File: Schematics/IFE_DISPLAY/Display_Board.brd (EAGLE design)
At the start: 108 x 83.8 mm, 76 parts, among them IC2 EP2C5T144, Q1 16MHz, Q2 MMBT3904L, Q3 16MHz, U1 MCP1826S-1802E/DB, U10 TPS5420D, U2 EPCS1SI8N, U4 HEX_CONVERTER, U5 HEX_CONVERTER, U9 TPS5420D

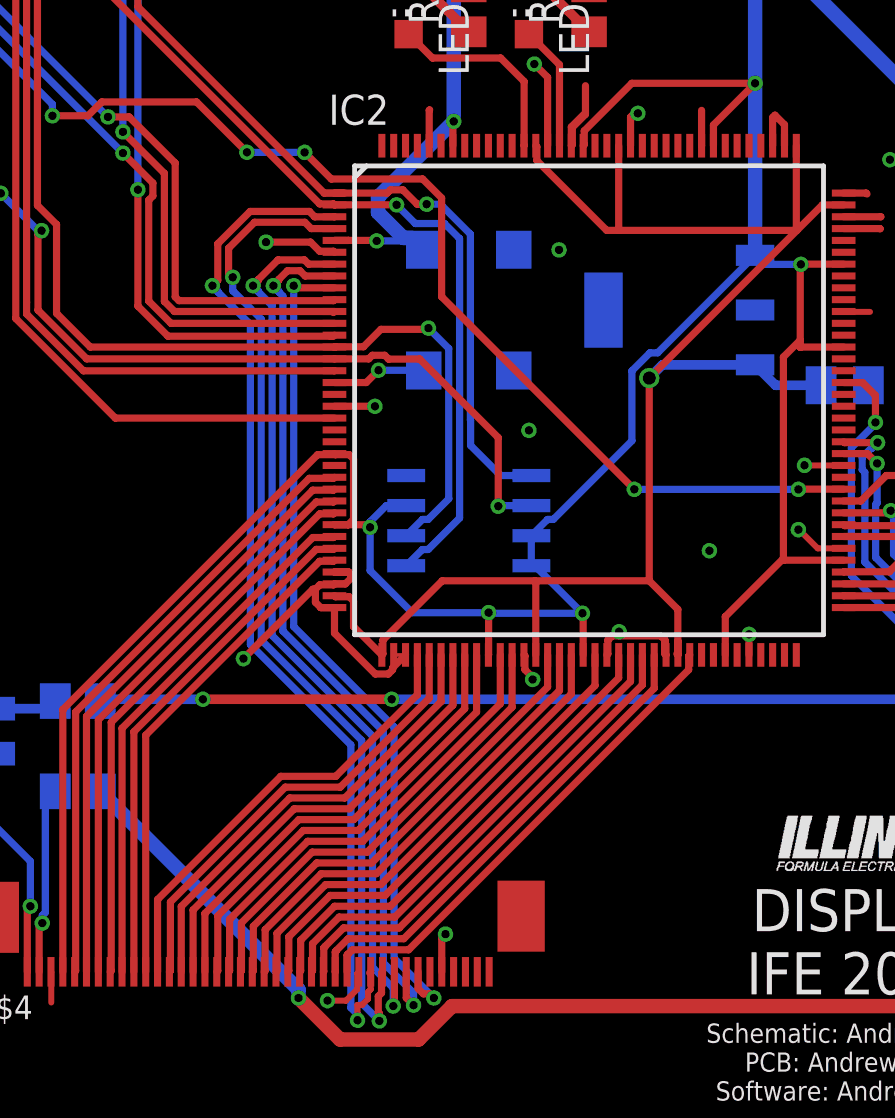
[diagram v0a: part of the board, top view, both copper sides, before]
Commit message: Fixed some random clearance issues
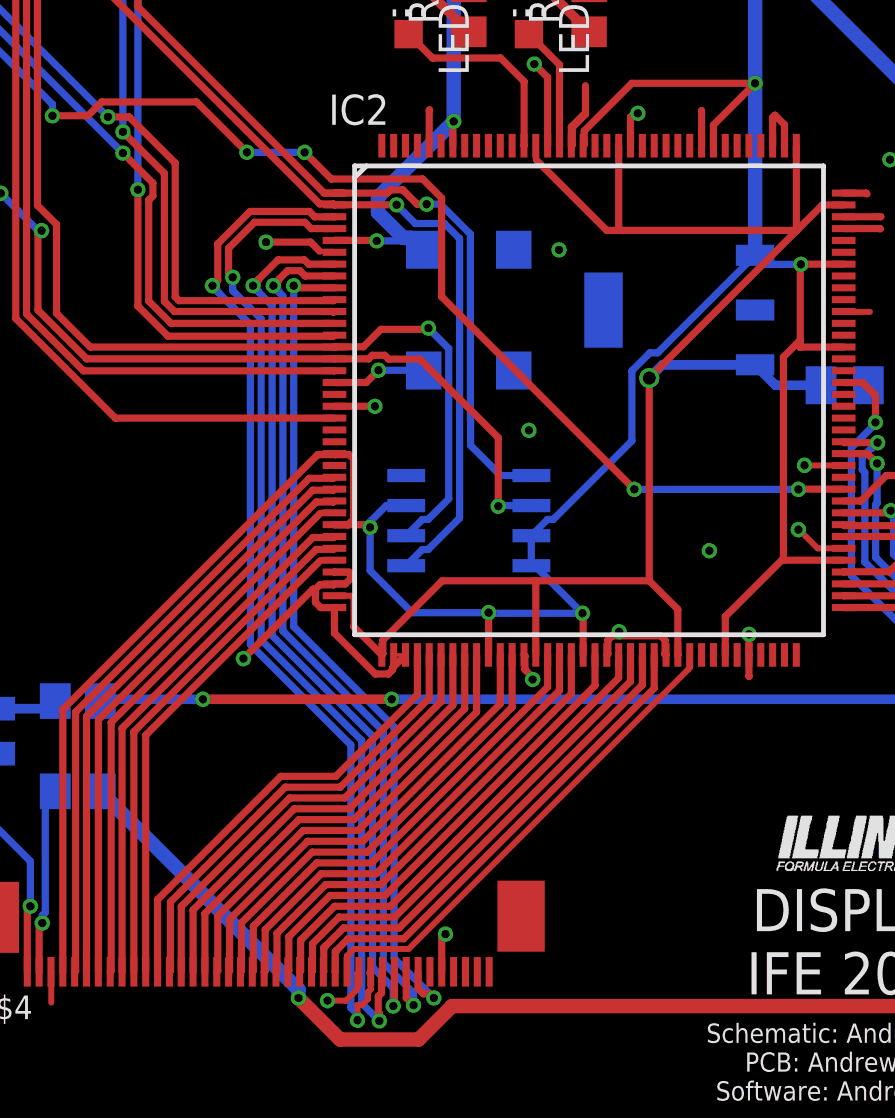
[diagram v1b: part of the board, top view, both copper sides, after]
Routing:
- net GND: track 73.5 -> 72.7 mm
- net VCC: track 71.7 -> 71.1 mm
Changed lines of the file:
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@@
 <wire x1="70.8406" y1="21.4884" x2="71.9582" y2="21.4884" width="0.4064" layer="1"/>
 <wire x1="71.9582" y1="21.4884" x2="73.533" y2="19.9136" width="0.4064" layer="1"/>
-<wire x1="29.89" y1="40.54" x2="29.8448" y2="40.5852" width="0.3048" layer="1"/>
-<wire x1="29.8448" y1="40.5852" x2="29.26375" y2="40.5852" width="0.3048" layer="1"/>
 <wire x1="28.87875" y1="40.9702" x2="27.0002" y2="40.9702" width="0.3048" layer="1"/>
-<wire x1="29.26375" y1="40.5852" x2="28.87875" y2="40.9702" width="0.3048" layer="1"/>
+<wire x1="28.87875" y1="40.9702" x2="29.26375" y2="40.5852" width="0.3048" layer="1"/>
 <via x="27.0002" y="40.9702" extent="1-16" drill="0.35"/>
 <wire x1="83.55" y1="43.18" x2="84.712625" y2="43.18" width="0.4064" layer="16"/>
@@
 <wire x1="29.26615" y1="26.4972" x2="29.0852" y2="26.31625" width="0.3048" layer="1"/>
 <wire x1="29.31135" y1="25.5376" x2="29.0852" y2="25.76375" width="0.3048" layer="1"/>
-<wire x1="29.89" y1="25.5376" x2="29.31135" y2="25.5376" width="0.3048" layer="1"/>
+<wire x1="29.89" y1="25.5376" x2="29.8876" y2="25.5376" width="0.3048" layer="1"/>
 <wire x1="32.3448" y1="22.91375" x2="32.16625" y2="22.7352" width="0.3048" layer="1"/>
 <wire x1="32.16625" y1="22.7352" x2="31.61375" y2="22.7352" width="0.3048" layer="1"/>
@@
 <wire x1="30.5816" y1="26.7716" x2="30.5816" y2="26.9494" width="0.3048" layer="1"/>
 <wire x1="30.4934" y1="27.0376" x2="30.5816" y2="26.9494" width="0.3048" layer="1"/>
-<wire x1="30.4934" y1="27.0376" x2="29.89" y2="27.0376" width="0.3048" layer="1"/>
+<wire x1="29.8924" y1="27.0376" x2="29.89" y2="27.0376" width="0.3048" layer="1"/>
 <wire x1="30.35" y1="26.54" x2="30.5816" y2="26.7716" width="0.3048" layer="1"/>
 <wire x1="41.61375" y1="24.3448" x2="41.91" y2="24.3448" width="0.3048" layer="1"/>
@@
 <wire x1="41.4328" y1="24.16385" x2="41.61375" y2="24.3448" width="0.3048" layer="1"/>
 <wire x1="43.66625" y1="24.3448" x2="43.8472" y2="24.16385" width="0.3048" layer="1"/>
-<wire x1="43.8472" y1="24.13" x2="43.8472" y2="24.16385" width="0.3048" layer="1"/>
-<wire x1="43.8472" y1="24.13" x2="43.8472" y2="23.5804" width="0.3048" layer="1"/>
+<wire x1="43.8472" y1="23.5828" x2="43.8472" y2="23.5804" width="0.3048" layer="1"/>
 <wire x1="41.91" y1="24.3448" x2="41.91" y2="24.5198" width="0.3048" layer="1"/>
 <via x="41.91" y="24.5198" extent="1-16" drill="0.35"/>
-<wire x1="47.39" y1="23.54" x2="47.39" y2="24.403" width="0.3048" layer="1"/>
+<wire x1="47.39" y1="24.403" x2="47.39" y2="23.54" width="0.3048" layer="1"/>
 <wire x1="47.39" y1="24.403" x2="47.3964" y2="24.4094" width="0.3048" layer="1"/>
 <via x="47.3964" y="24.4094" extent="1-16" drill="0.35"/>
@@
 <wire x1="39.9328" y1="45.81043125" x2="40.4876" y2="46.36523125" width="0.3048" layer="1"/>
 <wire x1="43.89" y1="23.54" x2="43.8472" y2="23.5828" width="0.3048" layer="1"/>
-<wire x1="43.8472" y1="23.5828" x2="43.8472" y2="24.13" width="0.3048" layer="1"/>
+<wire x1="43.8472" y1="23.5828" x2="43.8472" y2="24.16385" width="0.3048" layer="1"/>
 <wire x1="29.89" y1="34.04" x2="31.5936" y2="34.04" width="0.3048" layer="1"/>
 <wire x1="31.5936" y1="34.04" x2="31.5976" y2="34.036" width="0.3048" layer="1"/>
@@
 <via x="82.9056" y="25.654" extent="1-16" drill="0.35"/>
 <via x="67.945" y="33.1724" extent="1-16" drill="0.35"/>
+<wire x1="47.39" y1="23.54" x2="47.39" y2="22.6378" width="0.3048" layer="1"/>
+<wire x1="47.39" y1="22.6378" x2="47.3964" y2="22.6314" width="0.3048" layer="1"/>
+<wire x1="29.26375" y1="40.5852" x2="29.8448" y2="40.5852" width="0.2032" layer="1"/>
+<wire x1="29.8448" y1="40.5852" x2="29.89" y2="40.54" width="0.2032" layer="1"/>
 </signal>
 <signal name="+3V3">
@@
 <contactref element="U1" pad="3"/>
 <contactref element="C25" pad="1"/>
-<wire x1="30.6948" y1="25.81625" x2="30.51625" y2="25.9948" width="0.3048" layer="1"/>
-<wire x1="30.6948" y1="24.7352" x2="31.89" y2="23.54" width="0.3048" layer="1"/>
-<wire x1="30.51625" y1="25.9948" x2="29.9352" y2="25.9948" width="0.3048" layer="1"/>
-<wire x1="29.9352" y1="25.9948" x2="29.89" y2="26.04" width="0.3048" layer="1"/>
-<wire x1="30.6948" y1="24.7352" x2="30.6948" y2="25.81625" width="0.3048" layer="1"/>
+<wire x1="31.89" y1="23.54" x2="30.6948" y2="24.7352" width="0.3048" layer="1"/>
 <wire x1="31.89" y1="23.54" x2="31.9352" y2="23.5852" width="0.3048" layer="1"/>
 <wire x1="31.9352" y1="23.5852" x2="31.9352" y2="24.16625" width="0.3048" layer="1"/>
@@
 <wire x1="38.354" y1="26.67" x2="34.43895" y2="26.67" width="0.3048" layer="1"/>
 <wire x1="38.354" y1="26.67" x2="43.18" y2="26.67" width="0.3048" layer="1"/>
-<wire x1="44.3448" y1="23.5852" x2="44.3876" y2="23.5424" width="0.3048" layer="1"/>
 <wire x1="38.39" y1="23.54" x2="38.39" y2="26.634" width="0.3048" layer="1"/>
 <wire x1="38.39" y1="26.634" x2="38.354" y2="26.67" width="0.3048" layer="1"/>
@@
 <wire x1="49.39" y1="41.4912" x2="49.39" y2="45.04" width="0.3048" layer="1"/>
 <wire x1="49.39" y1="41.4912" x2="49.4157" y2="41.4655" width="0.3048" layer="1"/>
-<wire x1="38.39" y1="45.04" x2="38.4352" y2="44.9948" width="0.3048" layer="1"/>
-<wire x1="38.4352" y1="44.9948" x2="38.4352" y2="44.41375" width="0.3048" layer="1"/>
-<wire x1="38.4352" y1="44.41375" x2="41.38345" y2="41.4655" width="0.3048" layer="1"/>
+<wire x1="41.38345" y1="41.4655" x2="38.4352" y2="44.41375" width="0.3048" layer="1"/>
 <wire x1="41.91" y1="41.4655" x2="41.38345" y2="41.4655" width="0.3048" layer="1"/>
 <wire x1="41.91" y1="41.4655" x2="49.4157" y2="41.4655" width="0.3048" layer="1"/>
@@
 <wire x1="48.514" y1="34.925" x2="50.435" y2="34.925" width="0.4064" layer="16"/>
 <wire x1="43.18" y1="26.67" x2="44.3876" y2="25.4624" width="0.3048" layer="1"/>
-<wire x1="44.3876" y1="24.13" x2="44.3876" y2="25.4624" width="0.3048" layer="1"/>
-<wire x1="44.3876" y1="24.13" x2="44.3876" y2="23.54" width="0.3048" layer="1"/>
+<wire x1="44.3876" y1="23.5424" x2="44.3876" y2="25.4624" width="0.3048" layer="1"/>
+<wire x1="44.3876" y1="23.5424" x2="44.3876" y2="23.54" width="0.3048" layer="1"/>
 <wire x1="44.39" y1="23.54" x2="44.3876" y2="23.5424" width="0.3048" layer="1"/>
-<wire x1="44.3876" y1="23.5424" x2="44.3876" y2="24.13" width="0.3048" layer="1"/>
+<wire x1="38.4352" y1="44.41375" x2="38.39" y2="44.45895" width="0.254" layer="1"/>
+<wire x1="38.39" y1="44.45895" x2="38.39" y2="45.04" width="0.254" layer="1"/>
+<wire x1="30.6948" y1="24.7352" x2="30.6948" y2="25.9472" width="0.254" layer="1"/>
+<wire x1="30.602" y1="26.04" x2="29.89" y2="26.04" width="0.254" layer="1"/>
+<wire x1="30.6948" y1="25.9472" x2="30.602" y2="26.04" width="0.254" layer="1"/>
 </signal>
 <signal name="LED1">
@@
 <wire x1="20.4628" y1="10.2028" x2="20.4628" y2="20.69385" width="0.3048" layer="1"/>
 <wire x1="20.4628" y1="20.69385" x2="29.26375" y2="29.4948" width="0.3048" layer="1"/>
-<wire x1="29.26375" y1="29.4948" x2="29.8448" y2="29.4948" width="0.3048" layer="1"/>
-<wire x1="29.8448" y1="29.4948" x2="29.89" y2="29.54" width="0.3048" layer="1"/>
+<wire x1="29.26375" y1="29.4948" x2="29.30895" y2="29.54" width="0.254" layer="1"/>
+<wire x1="29.30895" y1="29.54" x2="29.89" y2="29.54" width="0.254" layer="1"/>
 </signal>
 <signal name="RED_4">
@@
 <contactref element="U$4" pad="P$11"/>
 <contactref element="IC2" pad="32"/>
-<wire x1="29.89" y1="27.54" x2="29.8448" y2="27.4948" width="0.3048" layer="1"/>
-<wire x1="29.8448" y1="27.4948" x2="29.26375" y2="27.4948" width="0.3048" layer="1"/>
-<wire x1="29.26375" y1="27.4948" x2="21.92" y2="20.15105" width="0.3048" layer="1"/>
+<wire x1="21.92" y1="20.15105" x2="29.26375" y2="27.4948" width="0.3048" layer="1"/>
 <wire x1="21.92" y1="20.15105" x2="21.92" y2="10.16" width="0.3048" layer="1"/>
+<wire x1="29.26375" y1="27.4948" x2="29.30895" y2="27.54" width="0.254" layer="1"/>
+<wire x1="29.30895" y1="27.54" x2="29.89" y2="27.54" width="0.254" layer="1"/>
 </signal>
 <signal name="RED_7">
@@
 <contactref element="U$4" pad="P$28"/>
 <contactref element="IC2" pad="63"/>
-<wire x1="44.89" y1="23.54" x2="44.8448" y2="23.4948" width="0.3048" layer="1"/>
-<wire x1="44.8448" y1="23.4948" x2="44.8448" y2="22.91375" width="0.3048" layer="1"/>
-<wire x1="30.64375" y1="11.0898" x2="30.4652" y2="10.91125" width="0.3048" layer="1"/>
-<wire x1="30.4652" y1="10.91125" x2="30.4652" y2="10.9072" width="0.3048" layer="1"/>
-<wire x1="44.8448" y1="22.91375" x2="33.02085" y2="11.0898" width="0.3048" layer="1"/>
-<wire x1="33.02085" y1="11.0898" x2="30.64375" y2="11.0898" width="0.3048" layer="1"/>
-<wire x1="30.42" y1="10.862" x2="30.42" y2="10.16" width="0.3048" layer="1"/>
-<wire x1="30.4652" y1="10.9072" x2="30.42" y2="10.862" width="0.3048" layer="1"/>
+<wire x1="30.42" y1="10.16" x2="30.42" y2="10.8366" width="0.254" layer="1"/>
+<wire x1="30.42" y1="10.8366" x2="30.7086" y2="11.1252" width="0.254" layer="1"/>
+<wire x1="44.8194" y1="22.92426875" x2="44.8194" y2="22.9246" width="0.254" layer="1"/>
+<wire x1="30.7086" y1="11.1252" x2="33.02033125" y2="11.1252" width="0.254" layer="1"/>
+<wire x1="33.02033125" y1="11.1252" x2="44.8194" y2="22.92426875" width="0.254" layer="1"/>
+<wire x1="44.89" y1="22.9952" x2="44.89" y2="23.54" width="0.254" layer="1"/>
+<wire x1="44.8194" y1="22.9246" x2="44.89" y2="22.9952" width="0.254" layer="1"/>
 </signal>
 <signal name="FPGA_REG_SEL">
